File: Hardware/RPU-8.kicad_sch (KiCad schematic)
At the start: 5 parts

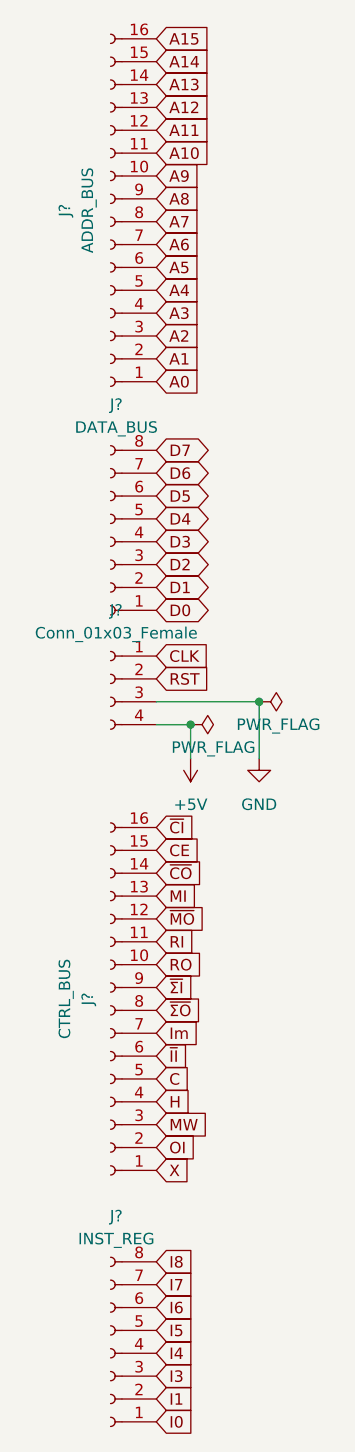
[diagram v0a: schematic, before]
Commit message: CTRL Board Layout Fixed
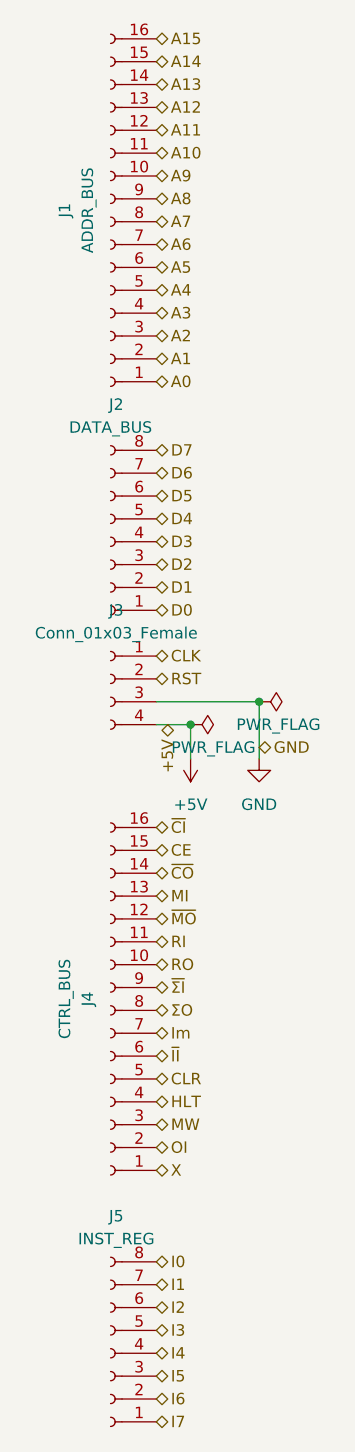
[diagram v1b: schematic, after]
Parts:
- gave numbers to parts that had none: 5
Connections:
- net I8 is gone; now on net I0: J5.8 (Pin_8)
- net I0: no longer J5.1 (Pin_1)
- net I1: now also J5.7 (Pin_7); no longer J5.2 (Pin_2)
- net I3: now also J5.5 (Pin_5); no longer J5.3 (Pin_3)
- net I5: now also J5.3 (Pin_3); no longer J5.5 (Pin_5)
- net I6: now also J5.2 (Pin_2); no longer J5.6 (Pin_6)
- net I7: now also J5.1 (Pin_1); no longer J5.7 (Pin_7)
- net C renamed CLR
- net H renamed HLT
- net ~{ΣO} renamed ΣO
- new net I2: J5.6 (Pin_6)
